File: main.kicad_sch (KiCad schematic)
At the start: 0 parts

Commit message: post solar meeting with ezzat
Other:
- added sheet Outputs (outputs.kicad_sch)
- sheet BMS ports: added BATT+, C6; removed none
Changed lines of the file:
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@@
 	(generator_version "9.0")
 	(paper "A4")
+	(wire
+		(pts
+			(xy 158.75 91.44) (xy 203.2 91.44)
+		)
+		(stroke
+			(width 0)
+			(type default)
+		)
+	)
 	(sheet
-		(at 39.37 80.01)
+		(at 203.2 82.55)
+		(size 12.7 29.21)
+		(exclude_from_sim no)
+		(in_bom yes)
+		(on_board yes)
+		(dnp no)
+		(fields_autoplaced yes)
+		(stroke
+			(width 0.1524)
+			(type solid)
+		)
+		(fill
+			(color 0 0 0 0.0000)
+		)
+		(property "Sheetname" "Outputs"
+			(at 203.2 81.8384 0)
+			(effects
+				(font
+					(size 1.27 1.27)
+				)
+				(justify left bottom)
+			)
+		)
+		(property "Sheetfile" "outputs.kicad_sch"
+			(at 203.2 112.3446 0)
+			(effects
+				(font
+					(size 1.27 1.27)
+				)
+				(justify left top)
+			)
+		)
+		(pin "BATT+" input
+			(at 203.2 91.44 180)
+			(effects
+				(font
+					(size 1.27 1.27)
+				)
+				(justify left)
+			)
+		)
+		(pin "BATT-" input
+			(at 203.2 99.06 180)
+			(effects
+				(font
+					(size 1.27 1.27)
+				)
+				(justify left)
+			)
+		)
+		(instances
+			(project "BMS"
+				(path "/124184ba-5d68-4d9f-8da6-acc6720ab30b/93f9b420-7cce-46a9-9201-666f07a18f85"
+					(page "2")
+				)
+			)
+		)
+	)
+	(sheet
+		(at 49.53 78.74)
 		(size 12.7 29.21)
 		(exclude_from_sim no)
@@
 		)
 		(property "Sheetname" "Inputs"
-			(at 39.37 79.2984 0)
+			(at 49.53 78.0284 0)
 			(effects
 				(font
@@
 		)
 		(property "Sheetfile" "input.kicad_sch"
-			(at 39.37 109.8046 0)
+			(at 49.53 108.5346 0)
 			(effects
 				(font
@@
 			)
 		)
-		(instances
-			(project "BMS"
-				(path "/124184ba-5d68-4d9f-8da6-acc6720ab30b/9364b786-ab76-48f0-917a-74b98e30a261"
-					(page "7")
-				)
-			)
-		)
 	)
 	(sheet
-		(at 120.65 90.17)
+		(at 120.65 87.63)
 		(size 38.1 15.24)
 		(exclude_from_sim no)
@@
 		)
 		(property "Sheetname" "BMS"
-			(at 120.65 89.4584 0)
+			(at 120.65 86.9184 0)
 			(effects
 				(font
@@
 		)
 		(property "Sheetfile" "controller.kicad_sch"
-			(at 120.65 105.9946 0)
+			(at 120.65 103.4546 0)
 			(effects
 				(font
@@
 			)
 		)
-		(instances
-			(project "BMS"
-				(path "/124184ba-5d68-4d9f-8da6-acc6720ab30b/9364b786-ab76-48f0-917a-74b98e30a261"
-					(page "5")
+		(pin "BATT+" output
+			(at 158.75 91.44 0)
+			(effects
+				(font
+					(size 1.27 1.27)
 				)
+				(justify right)
 			)
 		)
+		(pin "C6" input
+			(at 120.65 90.17 180)
+			(effects
+				(font
+					(size 1.27 1.27)
+				)
+				(justify left)
+			)
+		)

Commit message: almost done schematic
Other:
- sheet BMS: file controller.kicad_sch -> bossmodeshi.kicad_sch
- sheet BMS ports: added BATT-, C0, C1, C2, C3, C4, C5; removed none
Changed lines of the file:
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@@
+		)
+	)
+	(wire
+		(pts
+			(xy 158.75 99.06) (xy 203.2 99.06)
+		)
+		(stroke
+			(width 0)
+			(type default)
 		)
 	)
@@
 	(sheet
 		(at 120.65 87.63)
-		(size 38.1 15.24)
+		(size 38.1 17.78)
 		(exclude_from_sim no)
 		(in_bom yes)
@@
 			)
 		)
-		(property "Sheetfile" "controller.kicad_sch"
-			(at 120.65 103.4546 0)
+		(property "Sheetfile" "bossmodeshi.kicad_sch"
+			(at 120.65 105.9946 0)
 			(effects
 				(font
@@
 		)
 		(pin "C6" input
-			(at 120.65 90.17 180)
-			(effects
-				(font
-					(size 1.27 1.27)
-				)
-				(justify left)
-			)
-		)
+			(at 120.65 88.9 180)
+			(effects
+				(font
+					(size 1.27 1.27)
+				)
+				(justify left)
+			)
+		)
+		(pin "BATT-" output
+			(at 158.75 99.06 0)
+			(effects
+				(font
+					(size 1.27 1.27)
+				)
+				(justify right)
+			)
+		)
+		(pin "C5" input
+			(at 120.65 91.44 180)
+			(effects
+				(font
+					(size 1.27 1.27)
+				)
+				(justify left)
+			)
+		)
+		(pin "C0" input
+			(at 120.65 104.14 180)
+			(effects
+				(font
+					(size 1.27 1.27)
+				)
+				(justify left)
+			)
+		)
+		(pin "C1" input
+			(at 120.65 101.6 180)
+			(effects
+				(font
+					(size 1.27 1.27)
+				)
+				(justify left)
+			)
+		)
+		(pin "C2" input
+			(at 120.65 99.06 180)
+			(effects
+				(font
+					(size 1.27 1.27)
+				)
+				(justify left)
+			)
+		)
+		(pin "C3" input
+			(at 120.65 96.52 180)
+			(effects
+				(font
+					(size 1.27 1.27)
+				)
+				(justify left)
+			)
+		)
+		(pin "C4" input
+			(at 120.65 93.98 180)
+			(effects
+				(font
+					(size 1.27 1.27)
+				)
+				(justify left)
+			)
+		)
+		(instances
+			(project "BMS"
+				(path "/124184ba-5d68-4d9f-8da6-acc6720ab30b/93f9b420-7cce-46a9-9201-666f07a18f85"
+					(page "")
+				)
+			)
+		)

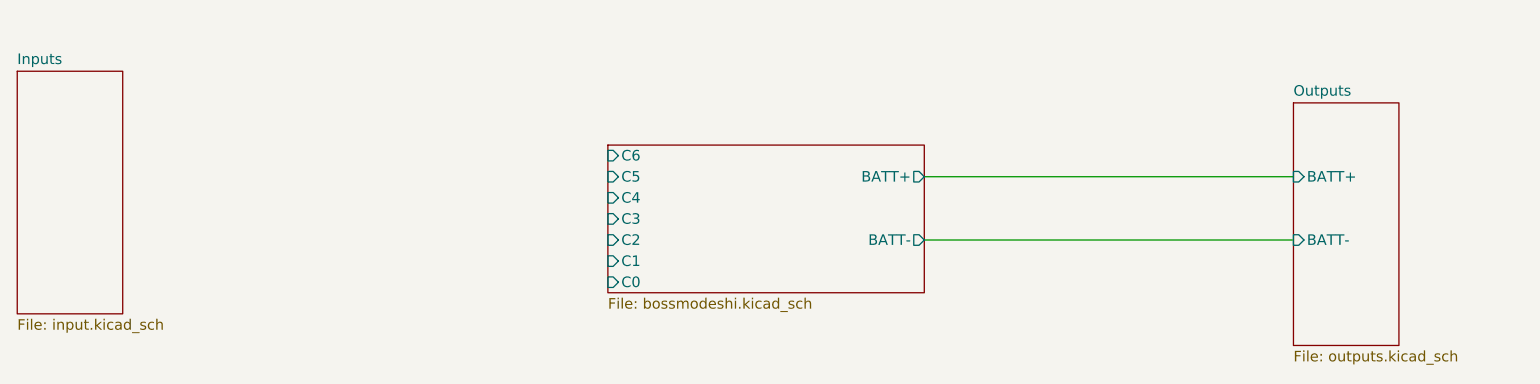
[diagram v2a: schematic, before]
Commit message: Fixing and cleaning up schematic
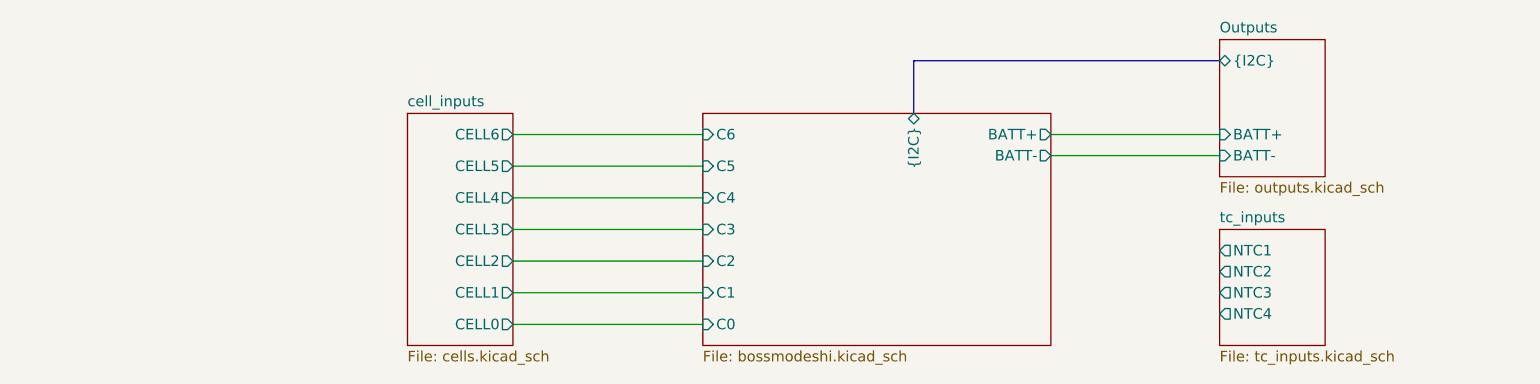
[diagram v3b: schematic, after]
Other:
- sheet Inputs renamed cell_inputs
- added sheet tc_inputs (tc_inputs.kicad_sch)
- sheet BMS ports: added {I2C}; removed none
- sheet Outputs ports: added {I2C}; removed none
- sheet cell_inputs: file input.kicad_sch -> cells.kicad_sch
- sheet cell_inputs ports: added CELL0, CELL1, CELL2, CELL3, CELL4, CELL5, CELL6; removed none

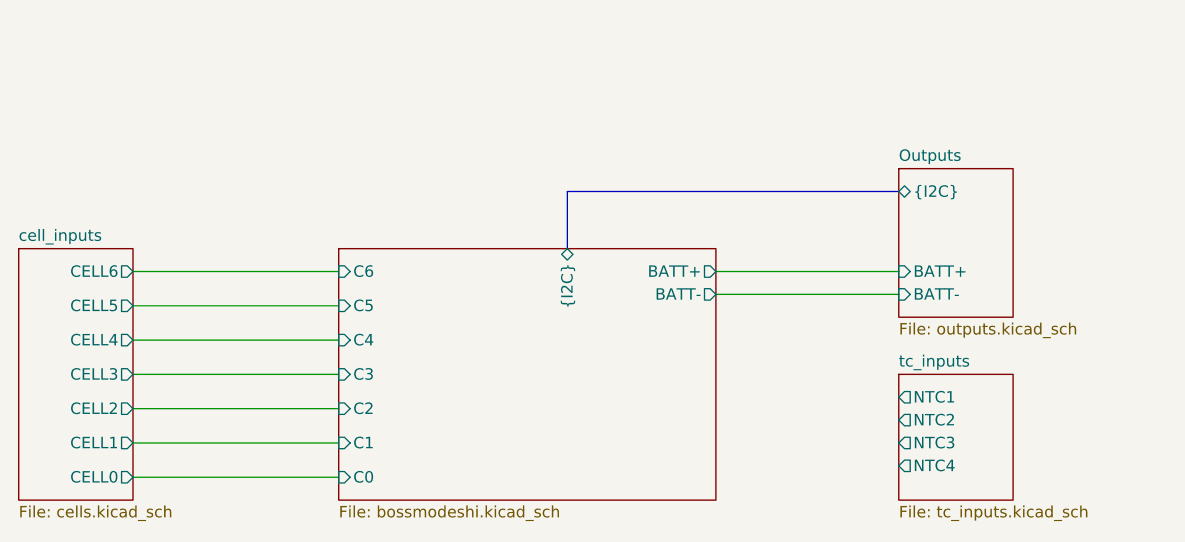
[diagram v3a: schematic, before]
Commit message: Reviewed and cleaned up schematic
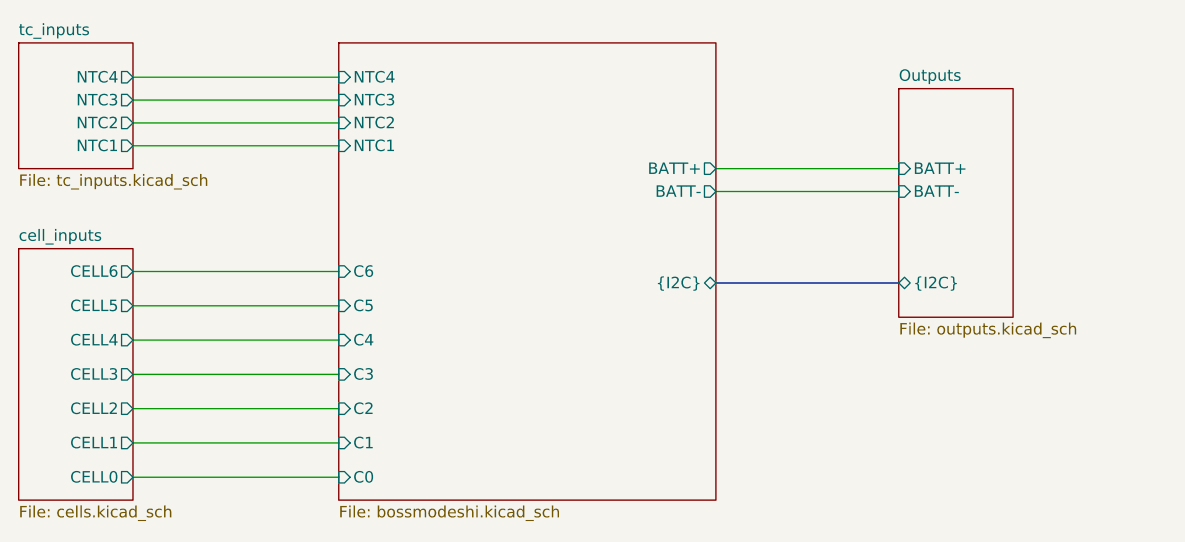
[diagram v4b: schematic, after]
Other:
- sheet BMS ports: added NTC1, NTC2, NTC3, NTC4; removed none
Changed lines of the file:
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@@
 	(wire
 		(pts
-			(xy 173.99 86.36) (xy 194.31 86.36)
-		)
-		(stroke
-			(width 0)
-			(type default)
-		)
-	)
-	(wire
-		(pts
-			(xy 173.99 88.9) (xy 194.31 88.9)
+			(xy 173.99 74.93) (xy 194.31 74.93)
+		)
+		(stroke
+			(width 0)
+			(type default)
+		)
+	)
+	(wire
+		(pts
+			(xy 173.99 77.47) (xy 194.31 77.47)
 		)
 		(stroke
@@
 		)
 	)
+	(wire
+		(pts
+			(xy 109.22 69.85) (xy 132.08 69.85)
+		)
+		(stroke
+			(width 0)
+			(type default)
+		)
+	)
+	(wire
+		(pts
+			(xy 109.22 93.98) (xy 132.08 93.98)
+		)
+		(stroke
+			(width 0)
+			(type default)
+		)
+	)
+	(wire
+		(pts
+			(xy 109.22 67.31) (xy 132.08 67.31)
+		)
+		(stroke
+			(width 0)
+			(type default)
+		)
+	)
+	(wire
+		(pts
+			(xy 109.22 101.6) (xy 132.08 101.6)
+		)
+		(stroke
+			(width 0)
+			(type default)
+		)
+	)
+	(wire
+		(pts
+			(xy 109.22 72.39) (xy 132.08 72.39)
+		)
+		(stroke
+			(width 0)
+			(type default)
+		)
+	)
+	(wire
+		(pts
+			(xy 109.22 105.41) (xy 132.08 105.41)
+		)
+		(stroke
+			(width 0)
+			(type default)
+		)
+	)
+	(wire
+		(pts
+			(xy 109.22 64.77) (xy 132.08 64.77)
+		)
+		(stroke
+			(width 0)
+			(type default)
+		)
+	)
+	(wire
+		(pts
+			(xy 109.22 109.22) (xy 132.08 109.22)
+		)
+		(stroke
+			(width 0)
+			(type default)
+		)
+	)
+	(wire
+		(pts
+			(xy 109.22 86.36) (xy 132.08 86.36)
+		)
+		(stroke
+			(width 0)
+			(type default)
+		)
+	)
 	(bus
 		(pts
-			(xy 157.48 77.47) (xy 157.48 83.82)
-		)
-		(stroke
-			(width 0)
-			(type default)
-		)
-	)
-	(wire
-		(pts
-			(xy 109.22 93.98) (xy 132.08 93.98)
-		)
-		(stroke
-			(width 0)
-			(type default)
-		)
-	)
-	(wire
-		(pts
-			(xy 109.22 101.6) (xy 132.08 101.6)
-		)
-		(stroke
-			(width 0)
-			(type default)
-		)
-	)
-	(bus
-		(pts
-			(xy 194.31 77.47) (xy 157.48 77.47)
-		)
-		(stroke
-			(width 0)
-			(type default)
-		)
-	)
-	(wire
-		(pts
-			(xy 109.22 105.41) (xy 132.08 105.41)
-		)
-		(stroke
-			(width 0)
-			(type default)
-		)
-	)
-	(wire
-		(pts
-			(xy 109.22 109.22) (xy 132.08 109.22)
-		)
-		(stroke
-			(width 0)
-			(type default)
-		)
-	)
-	(wire
-		(pts
-			(xy 109.22 86.36) (xy 132.08 86.36)
+			(xy 173.99 87.63) (xy 194.31 87.63)
 		)
 		(stroke
@@
 		(polyline
 			(pts
-				(xy 181.61 90.17) (xy 181.61 85.09) (xy 186.69 85.09) (xy 186.69 90.17)
+				(xy 181.61 78.74) (xy 181.61 73.66) (xy 186.69 73.66) (xy 186.69 78.74)
 			)
 			(stroke
@@
 		(length 2.54)
 		(shape round)
-		(at 184.15 85.09 0)
+		(at 184.15 73.66 0)
 		(fields_autoplaced yes)
 		(effects
@@
 		)
 		(property "Netclass" "HVBUS"
-			(at 184.8485 82.55 0)
+			(at 184.8485 71.12 0)
 			(effects
 				(font
@@
 		)
 		(property "Component Class" ""
-			(at -57.15 -15.24 0)
+			(at -57.15 -26.67 0)
 			(effects
 				(font
@@
 	)
 	(sheet
-		(at 194.31 74.93)
-		(size 12.7 16.51)
+		(at 194.31 66.04)
+		(size 12.7 25.4)
 		(exclude_from_sim no)
 		(in_bom yes)
@@
 		)
 		(property "Sheetname" "Outputs"
-			(at 194.31 74.2184 0)
+			(at 194.31 65.3284 0)
 			(effects
 				(font
@@
 		)
 		(pin "BATT+" input
-			(at 194.31 86.36 180)
+			(at 194.31 74.93 180)
 			(effects
 				(font
@@
 		)
 		(pin "BATT-" input
-			(at 194.31 88.9 180)
+			(at 194.31 77.47 180)
 			(effects
 				(font
@@
 		)
 		(pin "{I2C}" bidirectional
-			(at 194.31 77.47 180)
+			(at 194.31 87.63 180)
 			(effects
 				(font
@@
 	)
 	(sheet
-		(at 194.31 97.79)
+		(at 96.52 60.96)
 		(size 12.7 13.97)
 		(exclude_from_sim no)
@@
 		)
 		(property "Sheetname" "tc_inputs"
-			(at 194.31 97.0784 0)
+			(at 96.52 60.2484 0)
 			(effects
 				(font
@@
 		)
 		(property "Sheetfile" "tc_inputs.kicad_sch"
-			(at 194.31 112.3446 0)
+			(at 96.52 75.5146 0)
 			(effects
 				(font
@@
 		)
 		(pin "NTC1" output
-			(at 194.31 100.33 180)
-			(effects
-				(font
-					(size 1.27 1.27)
-				)
-				(justify left)
+			(at 109.22 72.39 0)
+			(effects
+				(font
+					(size 1.27 1.27)
+				)
+				(justify right)
 			)
 		)
 		(pin "NTC2" output
-			(at 194.31 102.87 180)
-			(effects
-				(font
-					(size 1.27 1.27)
-				)
-				(justify left)
+			(at 109.22 69.85 0)
+			(effects
+				(font
+					(size 1.27 1.27)
+				)
+				(justify right)
 			)
 		)
 		(pin "NTC3" output
-			(at 194.31 105.41 180)
-			(effects
-				(font
-					(size 1.27 1.27)
-				)
-				(justify left)
+			(at 109.22 67.31 0)
+			(effects
+				(font
+					(size 1.27 1.27)
+				)
+				(justify right)
 			)
 		)
 		(pin "NTC4" output
-			(at 194.31 107.95 180)
-			(effects
-				(font
-					(size 1.27 1.27)
-				)
-				(justify left)
+			(at 109.22 64.77 0)
+			(effects
+				(font
+					(size 1.27 1.27)
+				)
+				(justify right)
 			)
 		)
@@
 	)
 	(sheet
-		(at 132.08 83.82)
-		(size 41.91 27.94)
+		(at 132.08 60.96)
+		(size 41.91 50.8)
 		(exclude_from_sim no)
 		(in_bom yes)
@@
 		)
 		(property "Sheetname" "BMS"
-			(at 132.08 83.1084 0)
+			(at 132.08 60.2484 0)
 			(effects
 				(font
@@
 		)
 		(pin "BATT+" output
-			(at 173.99 86.36 0)
+			(at 173.99 74.93 0)
 			(effects
 				(font
@@
 		)
 		(pin "BATT-" output
-			(at 173.99 88.9 0)
+			(at 173.99 77.47 0)
 			(effects
 				(font
@@
 		)
 		(pin "{I2C}" bidirectional
-			(at 157.48 83.82 90)
-			(effects
-				(font
-					(size 1.27 1.27)
-				)
-				(justify right)
-			)
-		)
+			(at 173.99 87.63 0)
+			(effects
+				(font
+					(size 1.27 1.27)
+				)
+				(justify right)
+			)
+		)
+		(pin "NTC1" input
+			(at 132.08 72.39 180)
+			(effects
+				(font
+					(size 1.27 1.27)
+				)
+				(justify left)
+			)
+		)
+		(pin "NTC2" input
+			(at 132.08 69.85 180)
+			(effects
+				(font
+					(size 1.27 1.27)
+				)
+				(justify left)
+			)
+		)
+		(pin "NTC3" input
+			(at 132.08 67.31 180)
+			(effects
+				(font
+					(size 1.27 1.27)
+				)
+				(justify left)
+			)
+		)
+		(pin "NTC4" input
+			(at 132.08 64.77 180)
+			(effects
+				(font
+					(size 1.27 1.27)
+				)
+				(justify left)
+			)
+		)

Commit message: Working on microcontroller
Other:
- added sheet microcontroller (microcontroller.kicad_sch)
- added sheet usb (usb.kicad_sch)

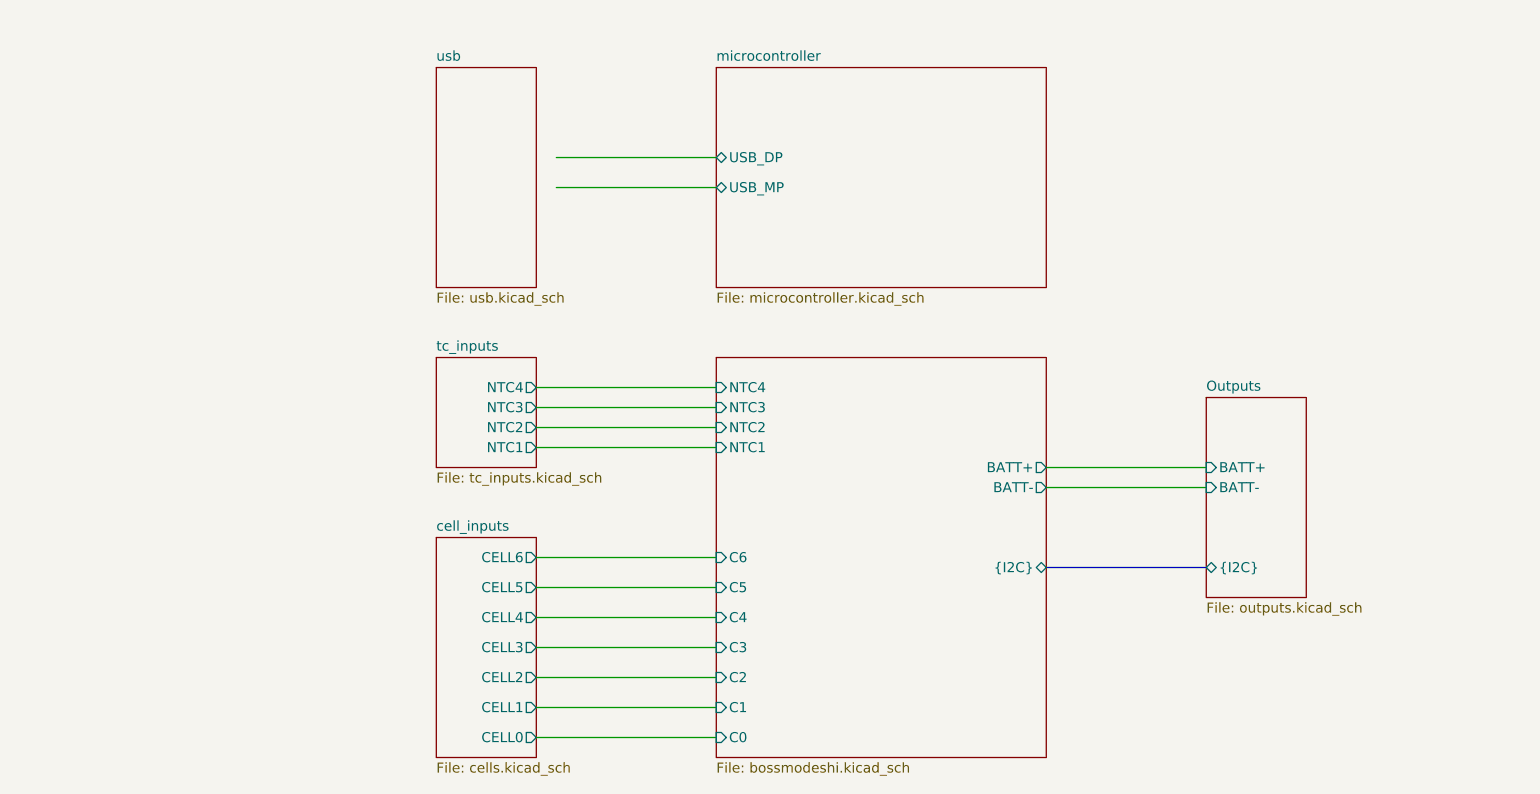
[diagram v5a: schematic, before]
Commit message: Updating schematic and adding in compnents to the PCB
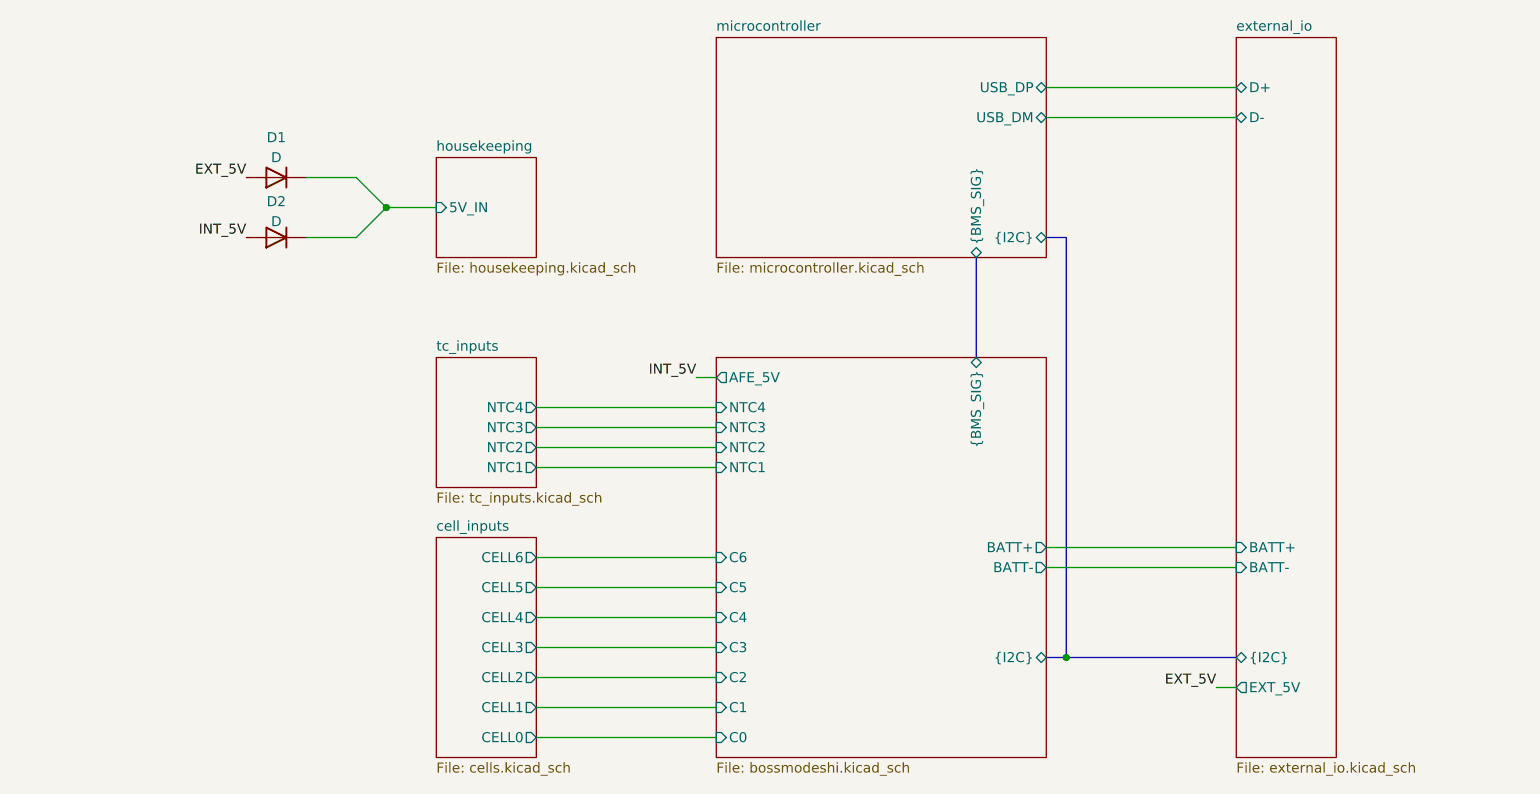
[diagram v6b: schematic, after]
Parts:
- added D1, D2: D, symbol Device:D
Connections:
- new net EXT_5V: D1.2 (A)
- new net INT_5V: D2.2 (A)
- new net housekeeping/5V_IN: D1.1 (K), D2.1 (K)
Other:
- sheet Outputs renamed external_io
- removed sheet usb
- added sheet housekeeping (housekeeping.kicad_sch)
- sheet BMS ports: added AFE_5V, {BMS_SIG}; removed none
- sheet external_io: file outputs.kicad_sch -> external_io.kicad_sch
- sheet external_io ports: added D+, D-, EXT_5V; removed none
- sheet microcontroller ports: added USB_DM, {BMS_SIG}, {I2C}; removed USB_MP

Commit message: Layed on board. Still need to route
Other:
- removed sheet tc_inputs
- sheet BMS ports: added PACK+, PACK-; removed C0, C6
- sheet cell_inputs ports: added BATT+, BATT-, NTC1, NTC2, NTC3, NTC4; removed CELL0, CELL6
- sheet external_io ports: added PACK+, PACK-; removed BATT+, BATT-
- moved on the sheet: D1, D2
